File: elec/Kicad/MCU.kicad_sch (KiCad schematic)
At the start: 15 parts, among them U1 STM32L053C8T6, Y1 32MHz

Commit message: merci charles de m'aider a nous aider
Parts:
- R19, R20: value 4K7 -> 10K
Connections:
- net XSHUT: now reaches U1.41 (PB5)
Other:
- moved on the sheet: R19
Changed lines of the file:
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@@
+	)
+	(junction
+		(at 73.66 119.38)
+		(diameter 0)
+		(color 0 0 0 0)
 	)
 	(junction
@@
 	)
 	(junction
-		(at 74.93 119.38)
-		(diameter 0)
-		(color 0 0 0 0)
-	)
-	(junction
 		(at 66.04 158.75)
 		(diameter 0)
@@
 	(wire
 		(pts
-			(xy 74.93 119.38) (xy 82.55 119.38)
-		)
-		(stroke
-			(width 0)
-			(type default)
-		)
-	)
-	(wire
-		(pts
 			(xy 29.21 119.38) (xy 29.21 120.65)
 		)
@@
 	(wire
 		(pts
-			(xy 74.93 110.49) (xy 74.93 109.22)
+			(xy 73.66 110.49) (xy 73.66 109.22)
 		)
 		(stroke
@@
 	(wire
 		(pts
+			(xy 73.66 119.38) (xy 82.55 119.38)
+		)
+		(stroke
+			(width 0)
+			(type default)
+		)
+	)
+	(wire
+		(pts
 			(xy 95.25 59.69) (xy 97.79 59.69)
 		)
@@
 	(wire
 		(pts
-			(xy 74.93 118.11) (xy 74.93 119.38)
+			(xy 73.66 118.11) (xy 73.66 119.38)
 		)
 		(stroke
@@
 	(wire
 		(pts
-			(xy 71.12 119.38) (xy 74.93 119.38)
+			(xy 71.12 119.38) (xy 73.66 119.38)
 		)
 		(stroke
@@
 	(wire
 		(pts
-			(xy 60.96 109.22) (xy 74.93 109.22)
+			(xy 60.96 109.22) (xy 73.66 109.22)
 		)
 		(stroke
@@
 		(property "Intersheetrefs" "${INTERSHEET_REFS}"
 			(at 76.34 66.04 0)
+			(effects
+				(font
+					(size 1.27 1.27)
+				)
+				(justify right)
+				(hide yes)
+			)
+		)
+	)
+	(global_label "XSHUT"
+		(shape output)
+		(at 82.55 111.76 180)
+		(fields_autoplaced yes)
+		(effects
+			(font
+				(size 1.016 1.016)
+			)
+			(justify right)
+		)
+		(property "Intersheetrefs" "${INTERSHEET_REFS}"
+			(at 75.324 111.76 0)
 			(effects
 				(font
@@
 			)
 		)
-		(property "Value" "4K7"
+		(property "Value" "10K"
 			(at 58.928 115.57 0)
 			(effects
@@
 	(symbol
 		(lib_id "Device:R")
-		(at 74.93 114.3 0)
+		(at 73.66 114.3 0)
 		(mirror y)
 		(unit 1)
@@
 		(dnp no)
 		(property "Reference" "R19"
-			(at 73.152 112.776 0)
-			(effects
-				(font
-					(size 1.27 1.27)
-				)
-				(justify left)
-			)
-		)
-		(property "Value" "4K7"
-			(at 73.152 115.57 0)
+			(at 71.882 112.776 0)
+			(effects
+				(font
+					(size 1.27 1.27)
+				)
+				(justify left)
+			)
+		)
+		(property "Value" "10K"
+			(at 71.882 115.57 0)
 			(effects
 				(font
@@
 		)
 		(property "Footprint" ""
-			(at 76.708 114.3 90)
+			(at 75.438 114.3 90)
 			(effects
 				(font
@@
 		)
 		(property "Datasheet" "https://www.digikey.ca/en/products/detail/vishay-dale/CRCW04021M00FKED/1178349"
-			(at 74.93 114.3 0)
+			(at 73.66 114.3 0)
 			(effects
 				(font
@@
 		)
 		(property "Description" ""
-			(at 74.93 114.3 0)
-			(effects
-				(font
+			(at 73.66 114.3 0)
+			(effects
+				(font

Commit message: multimetrie
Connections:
- net read_pin_high: now reaches U1.18 (PB0)
- net read_pin_low: now reaches U1.19 (PB1)
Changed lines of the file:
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@@
+		)
+	)
+	(global_label "read_pin_low"
+		(shape input)
+		(at 82.55 101.6 180)
+		(fields_autoplaced yes)
+		(effects
+			(font
+				(size 1.016 1.016)
+			)
+			(justify right)
+		)
+		(property "Intersheetrefs" "${INTERSHEET_REFS}"
+			(at 70.4376 101.6 0)
+			(effects
+				(font
+					(size 1.27 1.27)
+				)
+				(justify right)
+				(hide yes)
+			)
 		)
 	)
@@
 				(hide yes)
 			)
+		)
+	)
+	(global_label "read_pin_high"
+		(shape input)
+		(at 82.55 99.06 180)
+		(fields_autoplaced yes)
+		(effects
+			(font
+				(size 1.016 1.016)
+			)
+			(justify right)
+		)
+		(property "Intersheetrefs" "${INTERSHEET_REFS}"
+			(at 66.5022 99.06 0)
+			(effects
+				(font
+					(size 1.27 1.27)
+				)
+				(justify right)
+				(hide yes)
+			)

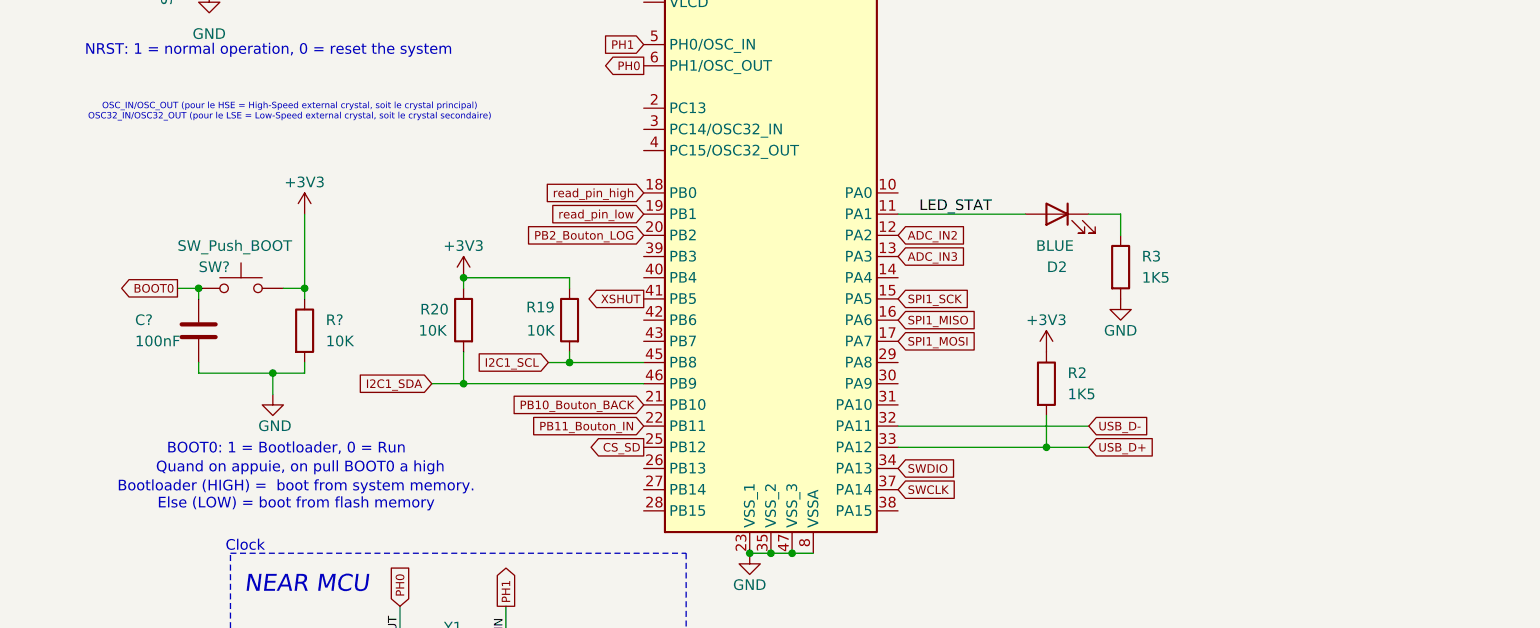
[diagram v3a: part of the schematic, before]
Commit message: push pour charles (début de l'ajout diviseur tension pour la batterie)
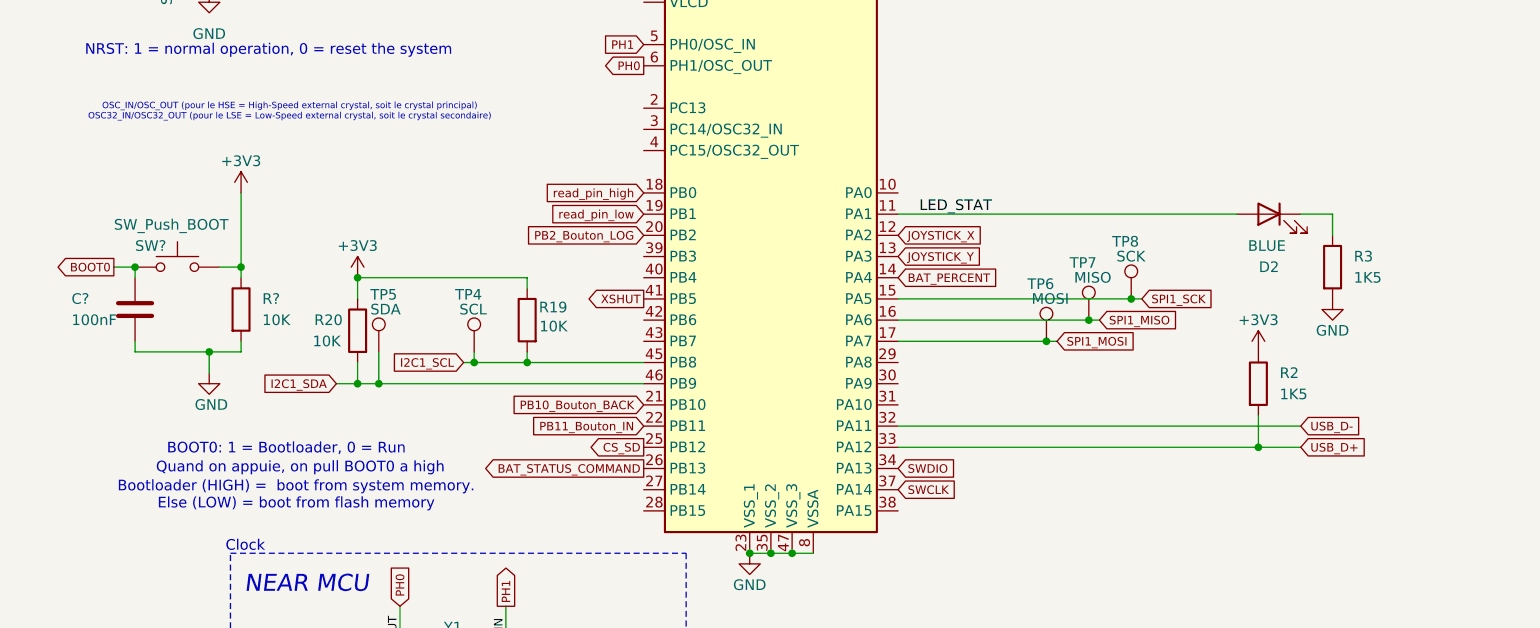
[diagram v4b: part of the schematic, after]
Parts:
- added TP4: SCL, symbol Connector:TestPoint
- added TP5: SDA, symbol Connector:TestPoint
- added TP6: MOSI, symbol Connector:TestPoint
- added TP7: MISO, symbol Connector:TestPoint
- added TP8: SCK, symbol Connector:TestPoint
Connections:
- net I2C1_SCL: now also TP4.1
- net I2C1_SDA: now also TP5.1
- net SPI1_MISO: now also TP7.1
- net SPI1_MOSI: now also TP6.1
- net SPI1_SCK: now also TP8.1
- net BAT_PERCENT: now reaches U1.14 (PA4)
- net BAT_STATUS_COMMAND: now reaches U1.26 (PB13)
- net ADC_IN2 renamed JOYSTICK_X
- net ADC_IN3 renamed JOYSTICK_Y
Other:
- moved on the sheet: C?, D2, R19, R2, R20, R3, R?, SW?

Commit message: push de magouille pour charles
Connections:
- net BAT_STATUS_COMMAND: no longer names the net of U1.26 (PB13)
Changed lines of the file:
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@@
-		)
-	)
-	(global_label "BAT_STATUS_COMMAND"
-		(shape output)
-		(at 82.55 132.08 180)
-		(fields_autoplaced yes)
-		(effects
-			(font
-				(size 1.016 1.016)
-			)
-			(justify right)
-		)
-		(property "Intersheetrefs" "${INTERSHEET_REFS}"
-			(at 63.1803 132.08 0)
-			(effects
-				(font
-					(size 1.27 1.27)
-				)
-				(justify right)
-				(hide yes)
-			)
 		)
 	)

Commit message: j'ai fait l'écran
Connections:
- net CS_LCD: now reaches U1.26 (PB13)
- net RESET_LCD: now reaches U1.39 (PB3)
- net RS_LCD: now reaches U1.40 (PB4)
- net BL_LCD: now reaches U1.42 (PB6)
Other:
- removed sheet Embedded ST-LINK V2-1
- note added: "Valider comment on envoie du code ici"
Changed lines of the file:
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@@
+		)
+	)
+	(text "Valider comment on envoie du code ici"
+		(exclude_from_sim no)
+		(at 140.97 133.096 0)
+		(effects
+			(font
+				(size 1.27 1.27)
+			)
 		)
 	)
@@
 		)
 	)
+	(global_label "RS_LCD"
+		(shape output)
+		(at 82.55 109.22 180)
+		(fields_autoplaced yes)
+		(effects
+			(font
+				(size 1.016 1.016)
+			)
+			(justify right)
+		)
+		(property "Intersheetrefs" "${INTERSHEET_REFS}"
+			(at 74.5499 109.22 0)
+			(effects
+				(font
+					(size 1.27 1.27)
+				)
+				(justify right)
+				(hide yes)
+			)
+		)
+	)
 	(global_label "SPI1_MOSI"
-		(shape input)
+		(shape output)
 		(at 132.08 116.84 0)
 		(fields_autoplaced yes)
@@
 	)
 	(global_label "SPI1_SCK"
-		(shape input)
+		(shape output)
 		(at 142.24 111.76 0)
 		(fields_autoplaced yes)
@@
 		)
 	)
+	(global_label "CS_LCD"
+		(shape output)
+		(at 82.55 132.08 180)
+		(fields_autoplaced yes)
+		(effects
+			(font
+				(size 1.016 1.016)
+			)
+			(justify right)
+		)
+		(property "Intersheetrefs" "${INTERSHEET_REFS}"
+			(at 74.5499 132.08 0)
+			(effects
+				(font
+					(size 1.27 1.27)
+				)
+				(justify right)
+				(hide yes)
+			)
+		)
+	)
 	(global_label "XSHUT"
 		(shape output)
@@
 	)
 	(global_label "I2C1_SCL"
-		(shape input)
+		(shape output)
 		(at 60.96 119.38 180)
 		(fields_autoplaced yes)
@@
 	)
 	(global_label "I2C1_SDA"
-		(shape input)
+		(shape bidirectional)
 		(at 45.72 121.92 180)
 		(fields_autoplaced yes)
@@
 		)
 		(property "Intersheetrefs" "${INTERSHEET_REFS}"
-			(at 36.2685 121.92 0)
+			(at 35.3795 121.92 0)
+			(effects
+				(font
+					(size 1.27 1.27)
+				)
+				(justify right)
+				(hide yes)
+			)
+		)
+	)
+	(global_label "BL_LCD"
+		(shape output)
+		(at 82.55 114.3 180)
+		(fields_autoplaced yes)
+		(effects
+			(font
+				(size 1.016 1.016)
+			)
+			(justify right)
+		)
+		(property "Intersheetrefs" "${INTERSHEET_REFS}"
+			(at 74.695 114.3 0)
 			(effects
 				(font
@@
 		)
 	)
+	(global_label "RESET_LCD"
+		(shape output)
+		(at 82.55 106.68 180)
+		(fields_autoplaced yes)
+		(effects
+			(font
+				(size 1.016 1.016)
+			)
+			(justify right)
+		)
+		(property "Intersheetrefs" "${INTERSHEET_REFS}"
+			(at 71.9374 106.68 0)
+			(effects
+				(font
+					(size 1.27 1.27)
+				)
+				(justify right)
+				(hide yes)
+			)
+		)
+	)
 	(symbol
 		(lib_id "Device:C")
@@
 				)
 			)
-		)
-	)
-	(sheet
-		(at 201.93 27.94)
-		(size 73.66 55.88)
-		(fields_autoplaced yes)
-		(stroke
-			(width 0.1524)
-			(type solid)
-		)
-		(fill
-			(color 0 0 0 0.0000)
-		)
-		(property "Sheetname" "Embedded ST-LINK V2-1"
-			(at 201.93 27.2284 0)
-			(effects
-				(font
-					(size 1.27 1.27)
-				)
-				(justify left bottom)
-			)
-		)
-		(property "Sheetfile" "ST-LINK.kicad_sch"
-			(at 201.93 84.4046 0)
-			(effects
-				(font
-					(size 1.27 1.27)
-				)
-				(justify left top)
-			)
-		)
-		(instances
-			(project "rulerSchematic"
-				(path "/a1545928-1195-40b9-b3c4-78f837012afb/47f0fc71-ff78-496f-bb04-036a9aeaa71c"
-					(page "9")
-				)
-			)

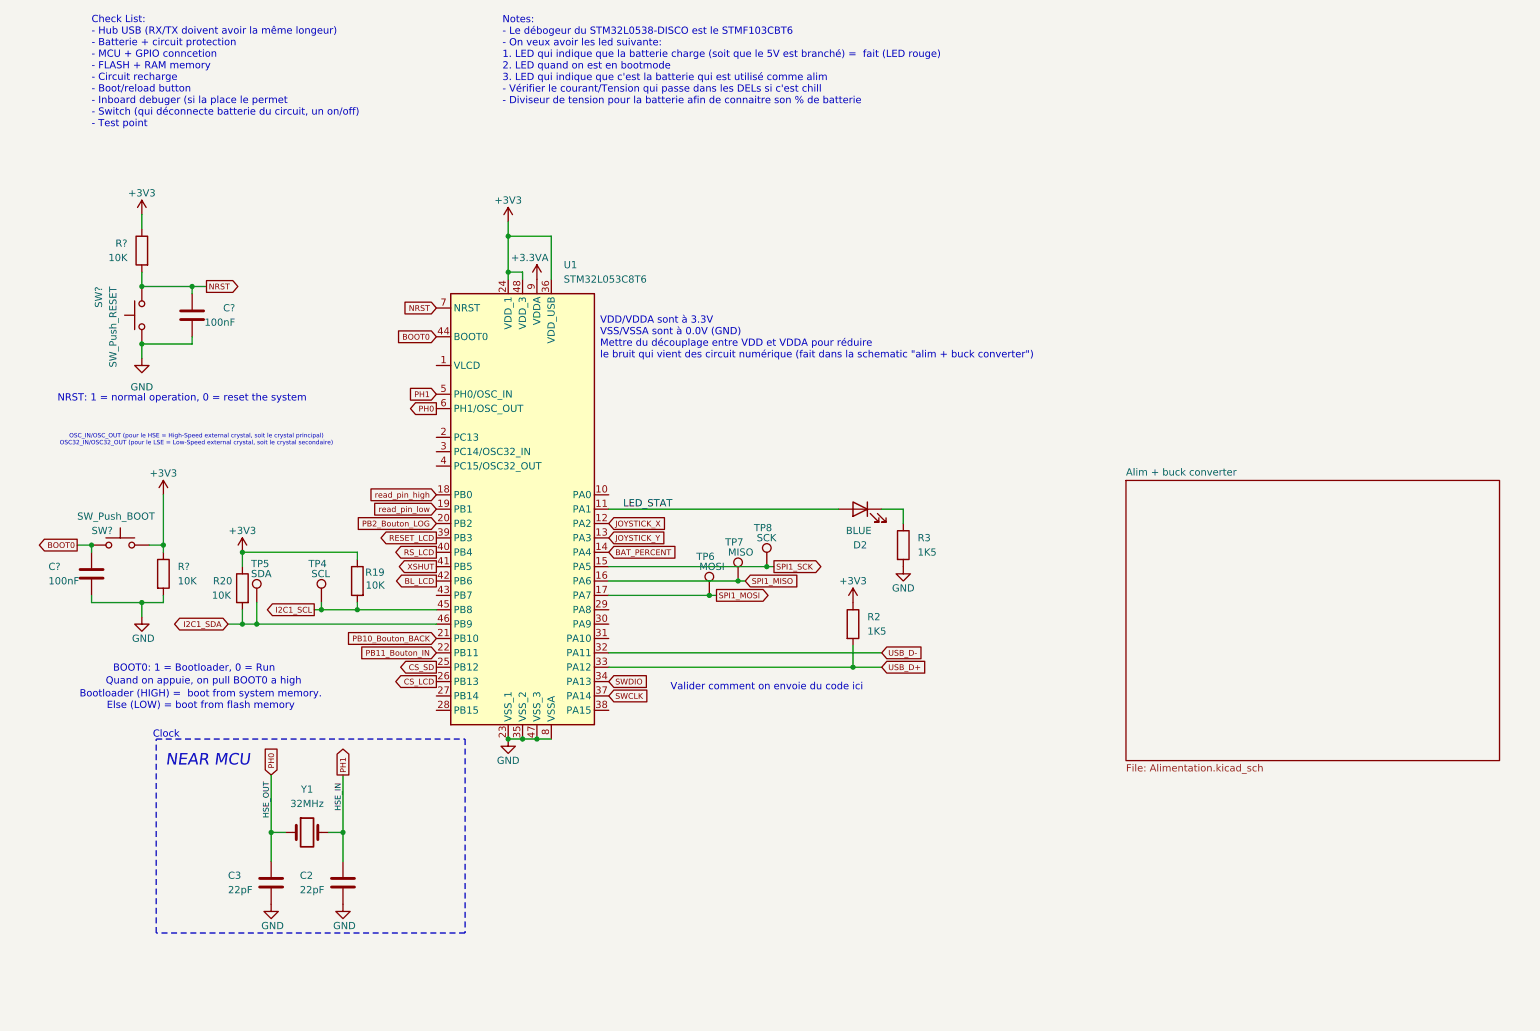
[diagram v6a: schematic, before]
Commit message: ajout de la LSE
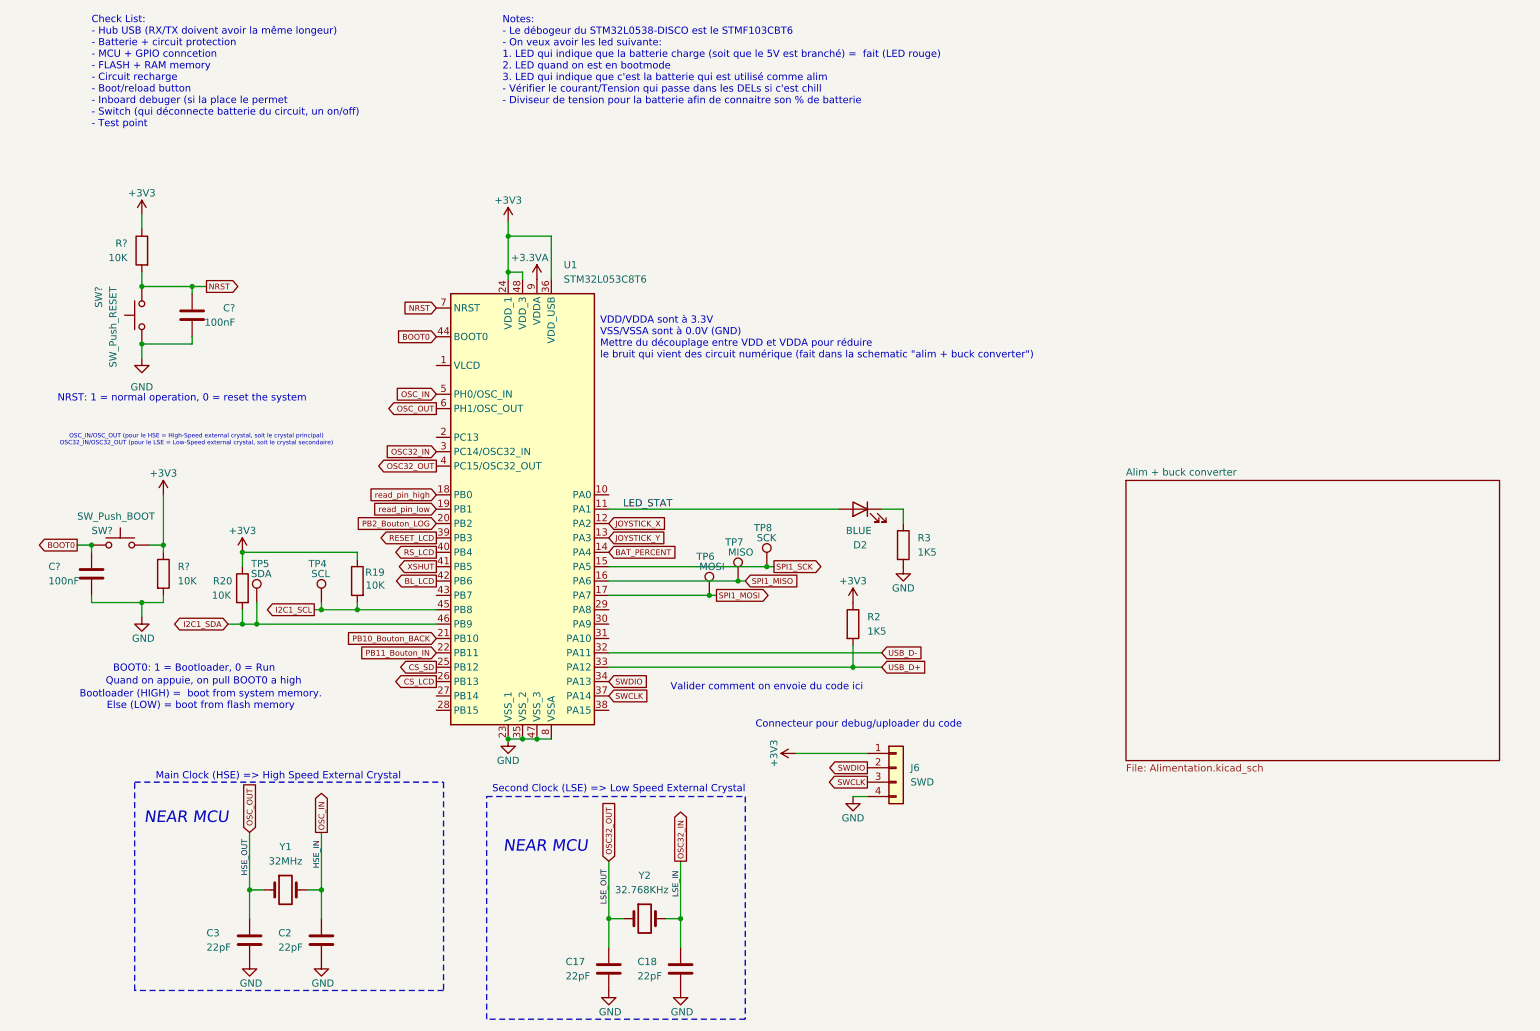
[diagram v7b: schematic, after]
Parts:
- added C17, C18: 22pF, symbol Device:C
- added J6: SWD, Connector_PinHeader_1.00mm:PinHeader_1x04_P1.00mm_Vertical, symbol Connector_Generic:Conn_01x04
- added Y2: 32.768KHz, Crystal:Crystal_SMD_3215-2Pin_3.2x1.5mm, symbol Device:Crystal
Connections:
- net +3V3: now also J6.1 (Pin_1)
- net GND: now also C17.2, C18.2, J6.4 (Pin_4)
- net SWCLK: now also J6.3 (Pin_3)
- net SWDIO: now also J6.2 (Pin_2)
- net OSC32_IN: now reaches U1.3 (PC14/OSC32_IN)
- net OSC32_IN: now also C18.1, Y2.2
- net OSC32_OUT: now reaches U1.4 (PC15/OSC32_OUT)
- net OSC32_OUT: now also C17.1, Y2.1
- net PH0 renamed OSC_OUT
- net PH1 renamed OSC_IN
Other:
- note added: "Connecteur pour debug/uploader du code"
- note added: "Main Clock (HSE) => High Speed External Crystal"
- note added: "Second Clock (LSE) => Low Speed External Crystal"
- note removed: "Clock"
- moved on the sheet: C2, C3, Y1
